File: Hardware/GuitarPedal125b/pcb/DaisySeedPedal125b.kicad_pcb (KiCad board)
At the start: 4 copper layers, 60 x 94 mm, 80 parts, among them J1 Barrel_Jack_Switch, J2 AUDIO_IN_TRS, J3 MIDI IN JACK, J4 AUDIO_OUT_TRS, J5 MIDI OUT JACK, J6 Conn_01x20_Socket, J7 Conn_01x20_Socket, K1 G6K-2, K2 G6K-2, Q1 SS8050, U1 LD1117S50TR_SOT223, U2 MCP6004, U3 OPA1652AID, U4 H11L1, U5 CPC1018N, U6 CPC1018N, U7 OLED_DISPLAY_SSD1306_SPI

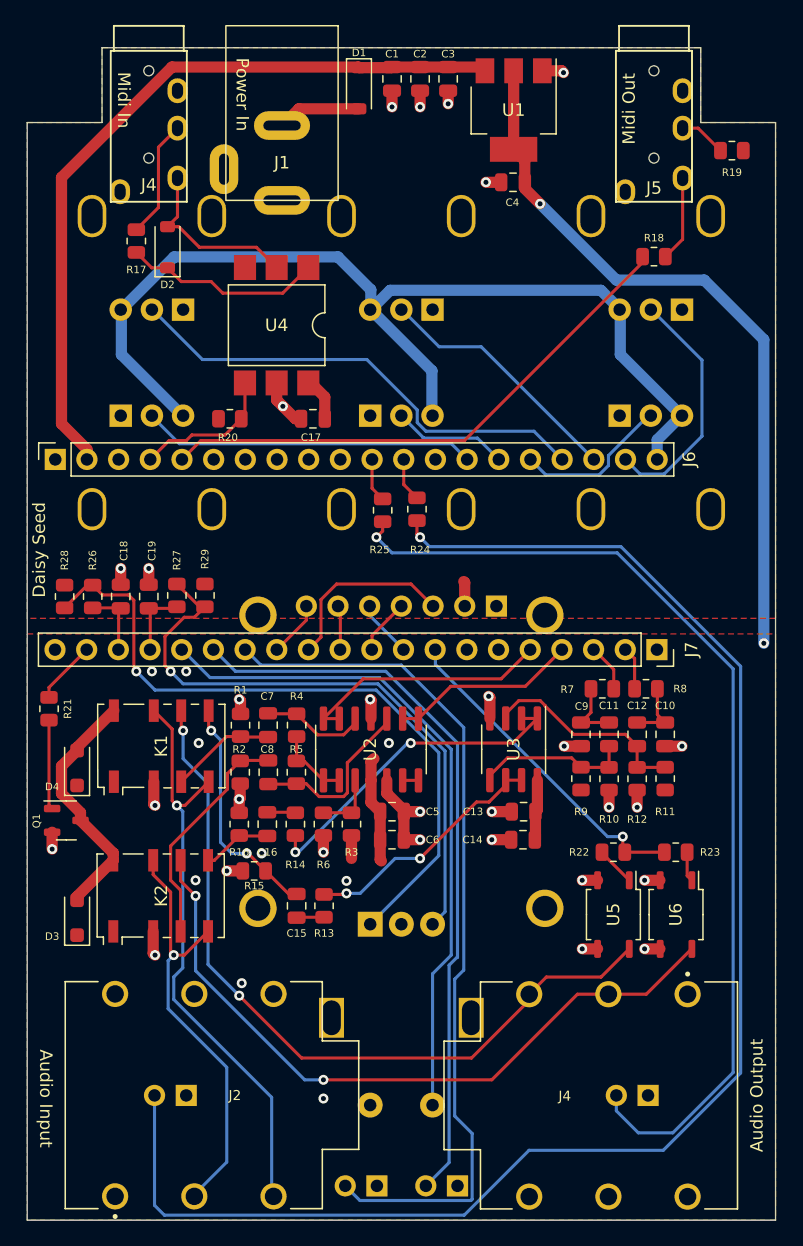
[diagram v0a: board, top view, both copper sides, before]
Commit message: Replace screen and encoder by 3 toggle switches and SD card reader.
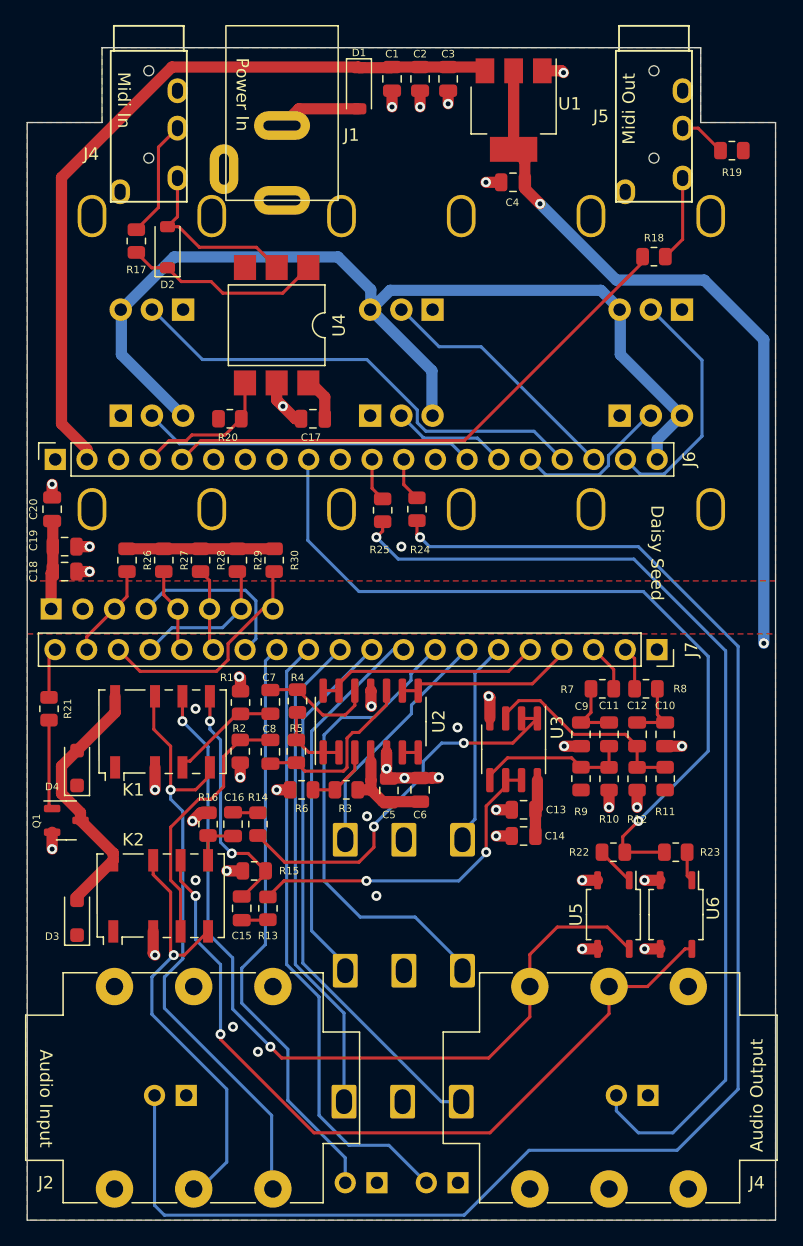
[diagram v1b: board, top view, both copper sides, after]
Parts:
- removed ENC1: RotaryEncoder_Switch, Rotary_Encoder:RotaryEncoder_Alps_EC11E-Switch_Vertical_H20mm
- removed U7: OLED_DISPLAY_SSD1306_SPI, GuitarPedal125B:HiLetgo_OLED_SPI
- added C20: 10UF, Capacitor_SMD:C_0805_2012Metric, F.Cu at (114.0, 78.0)
- added J8: Conn_01x08_Socket, Connector_PinHeader_2.54mm:PinHeader_1x08_P2.54mm_Vertical, B.Cu at (113.9, 86.0)
- added R30: 47K, Resistor_SMD:R_0805_2012Metric, F.Cu at (131.8, 82.1)
- added SW1: SW_SPDT_MSM, MyFootprints:MTS-103, B.Cu at (142.2, 120.5)
- added SW2: SW_SPDT_MSM, MyFootprints:MTS-103, B.Cu at (142.1, 131.0)
- added SW3: SW_SPDT_MSM, MyFootprints:MTS-103, B.Cu at (142.2, 110.0)
- C18: value 10NF -> 100NF
- C19: value 10NF -> 1UF
- J2, J4: footprint NMJ6HCD2:NEUTRIK_NMJ6HCD2 -> Connector_Audio:Jack_6.35mm_Neutrik_NMJ6HCD2_Horizontal
- R26, R27, R28, R29: value 10K -> 47K
- moved R28 11.3 mm to (125.9, 82.1)
- moved J4 10.8 mm to (152.3, 116.3)
- moved J2 9.81 mm to (131.7, 132.5)
- moved C19 7.85 mm to (115.0, 81.0), turned to 0 degrees
- moved FS1 6.50 mm to (146.5, 132.0)
- moved FS2 6.46 mm to (140.0, 132.0)
- moved C18 4.92 mm to (115.0, 83.0), turned to 0 degrees
- moved C6 4.59 mm to (143.5, 100.5), turned to 90 degrees
- moved R13 4.50 mm to (131.3, 110.0)
- moved C15 4.40 mm to (129.2, 110.0)
- moved R26 4.01 mm to (120.0, 82.1), turned to -90 degrees
- moved R29 3.84 mm to (128.8, 82.1), turned to -90 degrees
- moved R6 3.26 mm to (134.0, 100.5), turned to 180 degrees
- moved R27 3.01 mm to (123.0, 82.1)
- moved R14 3.00 mm to (130.5, 103.2)
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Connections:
- C18 pad 1: ENCODER_1_A -> +3.3V
- C19 pad 1: GND -> +3.3V
- C19 pad 2: ENCODER_1_B -> GND
- J6 pad 9: unconnected-(J6-Pin_9-Pad9) -> ENABLE_AUDIO_MUTE
- J7 pad 10: OLED_DISPLAY_SPI_MOSI -> LEVER_2_LEFT
- J7 pad 11: OLED_DISPLAY_SPI_DC -> LEVER_2_RIGHT
- J7 pad 12: OLED_DISPLAY_SPI_SCK -> FOOT_SWITCH_1
- J7 pad 13: OLED_DISPLAY_SPI_CS -> FOOT_SWITCH_2
- J7 pad 14: FOOT_SWITCH_1 -> SD_CLK
- J7 pad 15: FOOT_SWITCH_2 -> SD_CMD
- J7 pad 16: ENCODER_1_CLICK -> SD_D0
- J7 pad 17: ENCODER_1_B -> SD_D1
- J7 pad 18: ENCODER_1_A -> SD_D2
- J7 pad 19: DISABLE_AUDIO_BYPASS -> SD_D3
- J7 pad 20: unconnected-(J7-Pin_20-Pad20) -> DISABLE_AUDIO_BYPASS
- J7 pad 6: unconnected-(J7-Pin_6-Pad6) -> LEVER_3_LEFT
- J7 pad 7: unconnected-(J7-Pin_7-Pad7) -> LEVER_3_RIGHT
- J7 pad 8: ENABLE_AUDIO_MUTE -> LEVER_1_LEFT
- J7 pad 9: OLED_DISPLAY_SPI_RESET -> LEVER_1_RIGHT
- R26 pad 1: ENCODER_1_A -> +3.3V
- R26 pad 2: Net-(ENC1-PadA) -> SD_D3
- R27 pad 1: Net-(ENC1-PadB) -> +3.3V
- R27 pad 2: ENCODER_1_B -> SD_D0
- R28 pad 2: Net-(ENC1-PadA) -> SD_CMD
- R29 pad 1: Net-(ENC1-PadB) -> +3.3V
- R29 pad 2: +3.3V -> SD_D1
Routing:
- net Net-(ENC1-PadA): track 55.6 -> 0.00 mm, vias 1 -> 0
- net ENCODER_1_CLICK: track 54.1 -> 0.00 mm
- net Net-(ENC1-PadB): track 49.1 -> 0.00 mm, vias 1 -> 0
- net LEVER_2_LEFT: track 0.00 -> 44.7 mm
- net LEVER_2_RIGHT: track 0.00 -> 39.3 mm
- net ENABLE_AUDIO_MUTE: track 26.4 -> 64.3 mm
- net LEVER_1_LEFT: track 0.00 -> 37.6 mm
- net LEVER_1_RIGHT: track 0.00 -> 29.9 mm
- net FOOT_SWITCH_1: track 69.5 -> 50.0 mm
- net SD_D2: track 0.00 -> 19.0 mm
- net LEVER_3_RIGHT: track 0.00 -> 18.6 mm
- net +3.3V: track 5.54 -> 22.5 mm
- net LEVER_3_LEFT: track 0.00 -> 16.2 mm
- net OLED_DISPLAY_SPI_SCK: track 14.6 -> 0.00 mm
- net SD_CLK: track 0.00 -> 14.0 mm
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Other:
- board text added: "Daisy Seed Guitar Pedal 125B (Rev 0) 16 Oct 2025"
- board text removed: "Daisy Seed Guitar Pedal 125B (Rev 6) Made by Keith Shepherd 2/25/2024"
